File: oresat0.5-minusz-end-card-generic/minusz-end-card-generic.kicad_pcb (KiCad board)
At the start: 4 copper layers, 99.8 x 94.6 mm, 28 parts, among them J2 Harwin M55-7101242R, J3 Harwin M55-7101242R, J4 Harwin M55-7101242R, J5 Harwin M55-7101242R

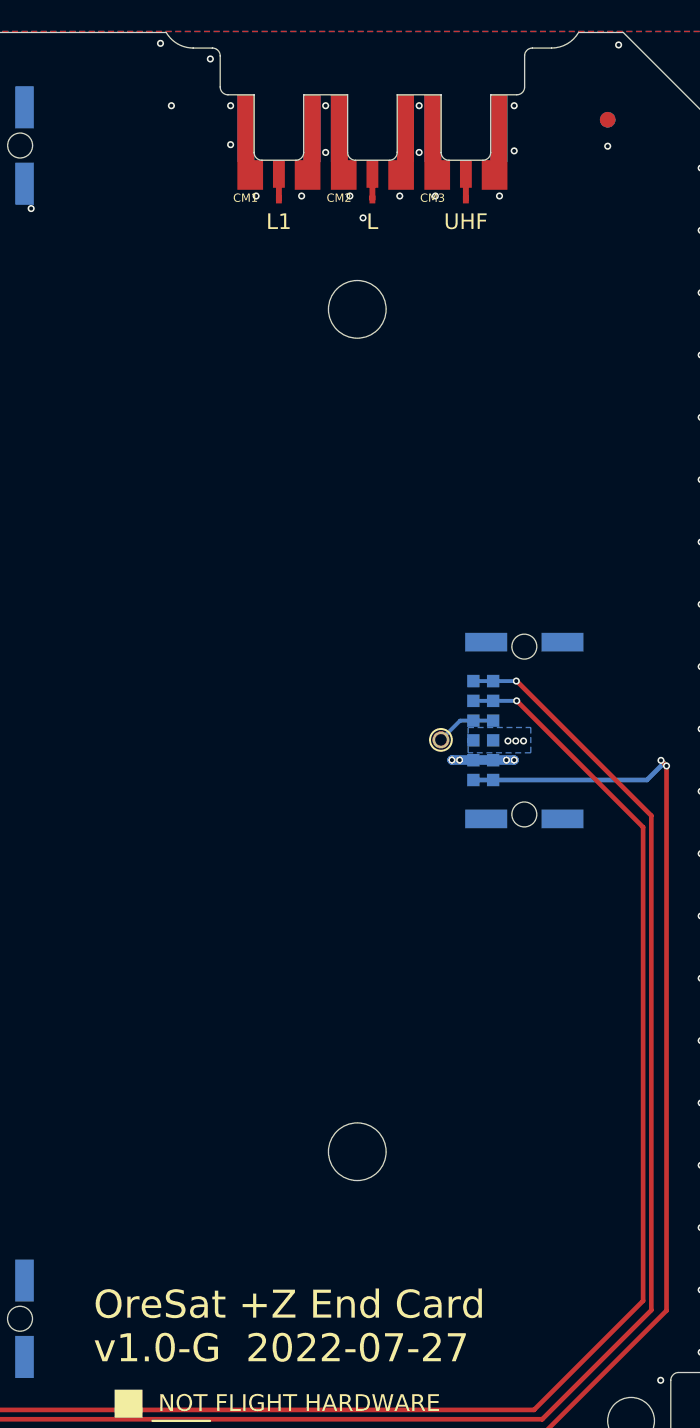
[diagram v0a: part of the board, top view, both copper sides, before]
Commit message: fix silkscreen for -z end card
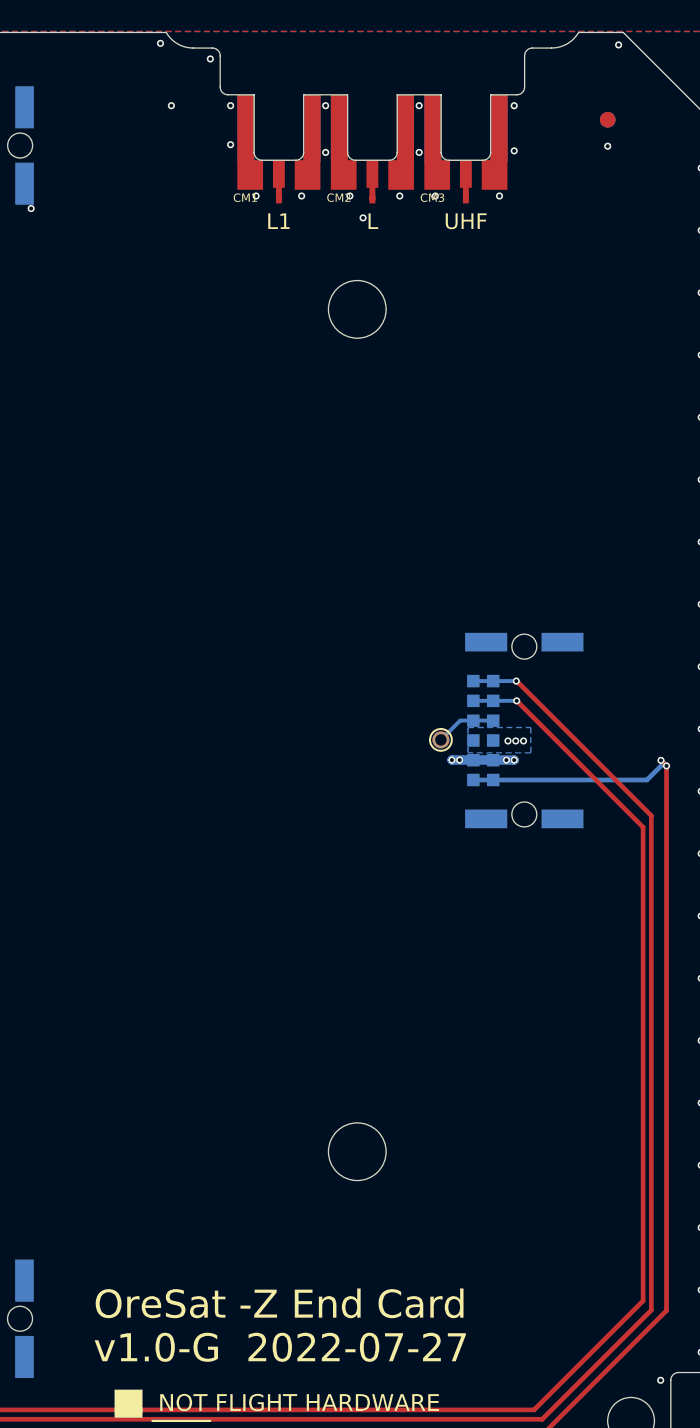
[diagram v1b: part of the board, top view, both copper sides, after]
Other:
- board text added: "OreSat -Z End Card"
- board text removed: "OreSat +Z End Card"
